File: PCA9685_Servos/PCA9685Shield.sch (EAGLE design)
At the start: 27 parts, among them U1 PCA9685

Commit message: Added OLED Shield Added LiPo Battery Charger Shield Updated outlines of all shields to match the cutout of the nodemcu board
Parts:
- JP7: value POWER_JACK1 -> POWER_JACKSMD; device SparkFun-Connectors:POWER_JACK1 -> SparkFun:POWER_JACKSMD
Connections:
- net GND: now also U$1.GND$10, U$1.GND$17, U$1.GND$24
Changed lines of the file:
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@@
 <?xml version="1.0" encoding="utf-8"?>
 <!DOCTYPE eagle SYSTEM "eagle.dtd">
-<eagle version="7.3.0">
+<eagle version="7.4.0">
 <drawing>
 <settings>
@@
 <part name="GND6" library="SparkFun" deviceset="GND" device=""/>
 <part name="P+2" library="SparkFun" deviceset="3.3V" device=""/>
-<part name="JP7" library="SparkFun-Connectors" deviceset="POWER_JACK" device="1"/>
+<part name="JP7" library="SparkFun" deviceset="POWER_JACK" device="SMD"/>
 <part name="GND7" library="SparkFun" deviceset="GND" device=""/>
 <part name="JP8" library="SparkFun" deviceset="M02" device="1X02_NO_SILK"/>
@@
 <part name="R7" library="SparkFun" deviceset="RESISTOR" device="0402-RES" value="10k"/>
 <part name="R8" library="SparkFun" deviceset="RESISTOR" device="0402-RES" value="10k"/>
+<part name="GND5" library="SparkFun" deviceset="GND" device=""/>
 </parts>
 <sheets>
@@
 <instance part="R7" gate="G$1" x="241.3" y="27.94" rot="R90"/>
 <instance part="R8" gate="G$1" x="246.38" y="27.94" rot="R90"/>
+<instance part="GND5" gate="1" x="73.66" y="17.78"/>
 </instances>
 <busses>
@@
 <wire x1="7.62" y1="33.02" x2="-5.08" y2="33.02" width="0.1524" layer="91"/>
 <wire x1="-5.08" y1="33.02" x2="-5.08" y2="20.32" width="0.1524" layer="91"/>
+<pinref part="U$1" gate="G$1" pin="GND$10"/>
+<wire x1="7.62" y1="43.18" x2="-5.08" y2="43.18" width="0.1524" layer="91"/>
+<wire x1="-5.08" y1="43.18" x2="-5.08" y2="33.02" width="0.1524" layer="91"/>
+<junction x="-5.08" y="33.02"/>
 </segment>
 <segment>
@@
 <junction x="172.72" y="137.16"/>
 </segment>
+<segment>
+<pinref part="U$1" gate="G$1" pin="GND$17"/>
+<pinref part="GND5" gate="1" pin="GND"/>
+<wire x1="71.12" y1="33.02" x2="73.66" y2="33.02" width="0.1524" layer="91"/>
+<wire x1="73.66" y1="33.02" x2="73.66" y2="20.32" width="0.1524" layer="91"/>
+<pinref part="U$1" gate="G$1" pin="GND$24"/>
+<wire x1="71.12" y1="50.8" x2="73.66" y2="50.8" width="0.1524" layer="91"/>
+<wire x1="73.66" y1="50.8" x2="73.66" y2="33.02" width="0.1524" layer="91"/>
+<junction x="73.66" y="33.02"/>
+</segment>
 </net>

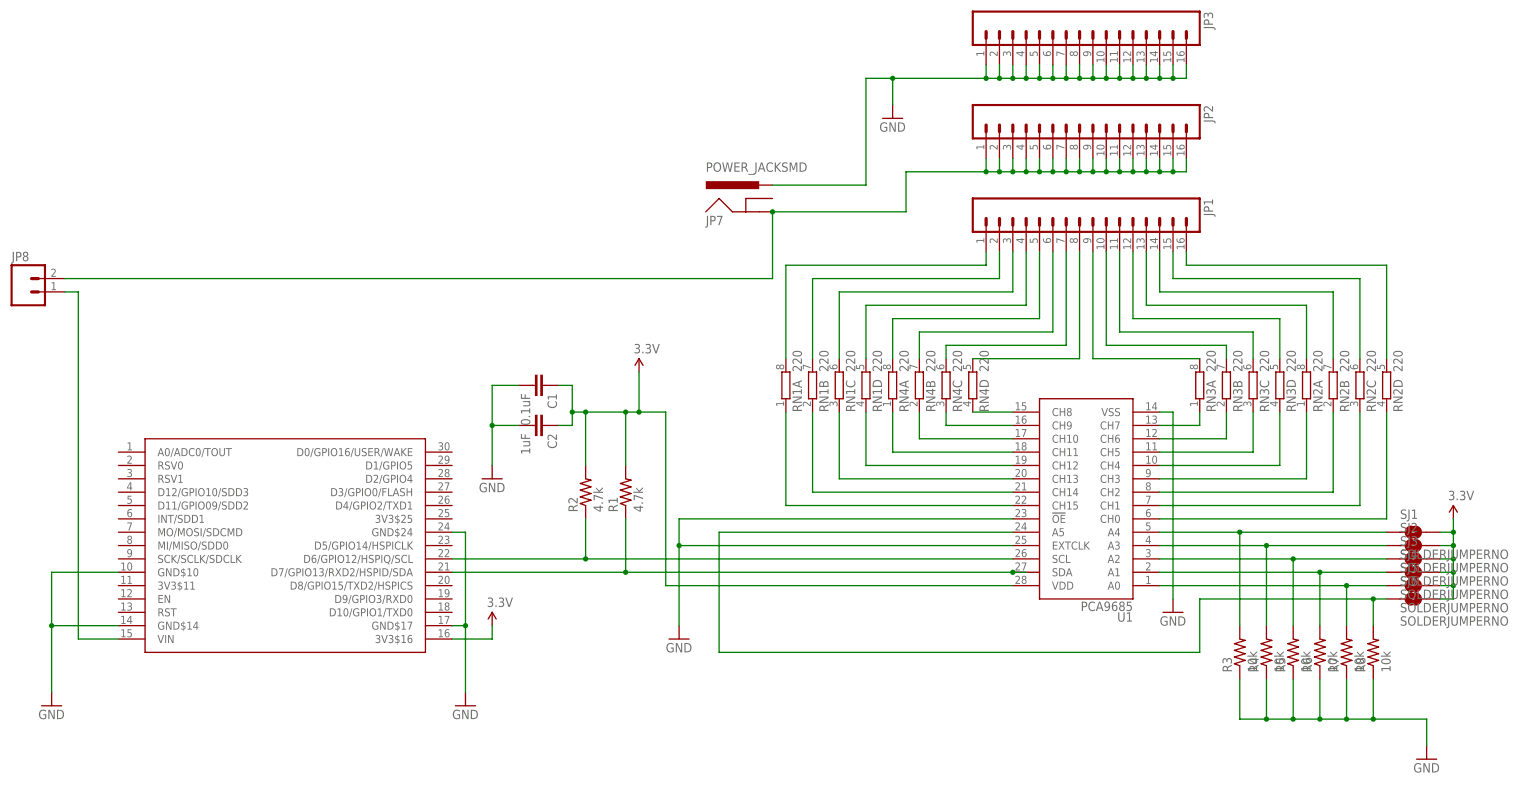
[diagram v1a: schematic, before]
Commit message: Updated the i2c pins to all shields to use d11/d12  as these pins will have dual use with the upcoming wifimcu Added FM24W256  Fram shield Added X95840 Digital potentiometer Shield Added AD5696 DAC Shield
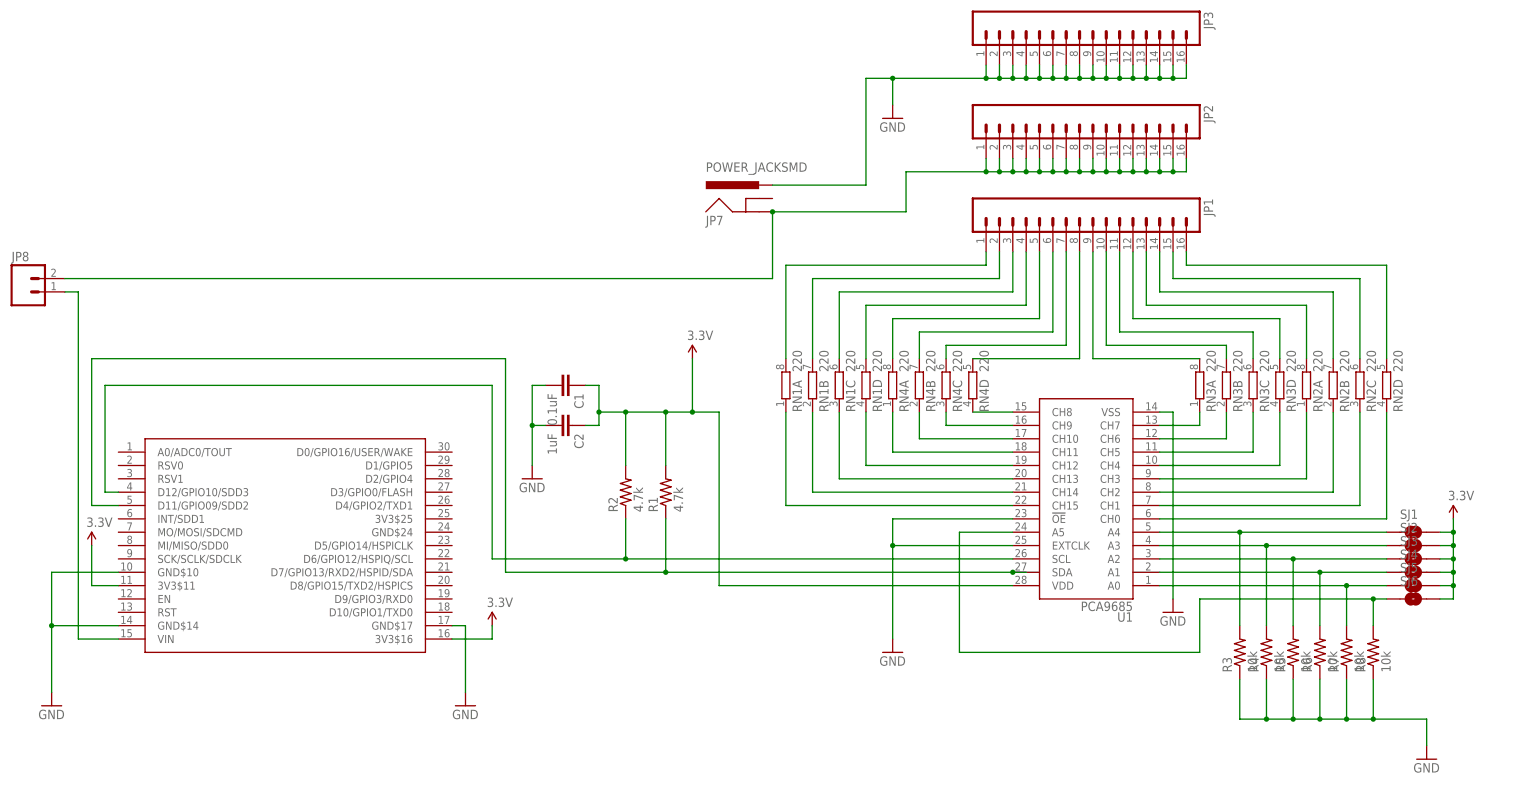
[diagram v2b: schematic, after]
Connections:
- net 3.3V: now also U$1.3V3$11
- net GND: no longer U$1.GND$24
- net N$2: now also U$1.D11/GPIO09/SDD2; no longer U$1.D7/GPIO13/RXD2/HSPID/SDA
- net N$8: now also U$1.D12/GPIO10/SDD3; no longer U$1.D6/GPIO12/HSPIQ/SCL
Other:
- moved on the sheet: C1, C2, R1, R2
